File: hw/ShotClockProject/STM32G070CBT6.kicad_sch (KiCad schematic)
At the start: 30 parts, among them J1 Conn_01x06_Pin, J2 Conn_ST_STDC14, SW1 SW_SPDT, U1 STM32G070CBTx, U2 LD39015M33R, Y1 16MHz

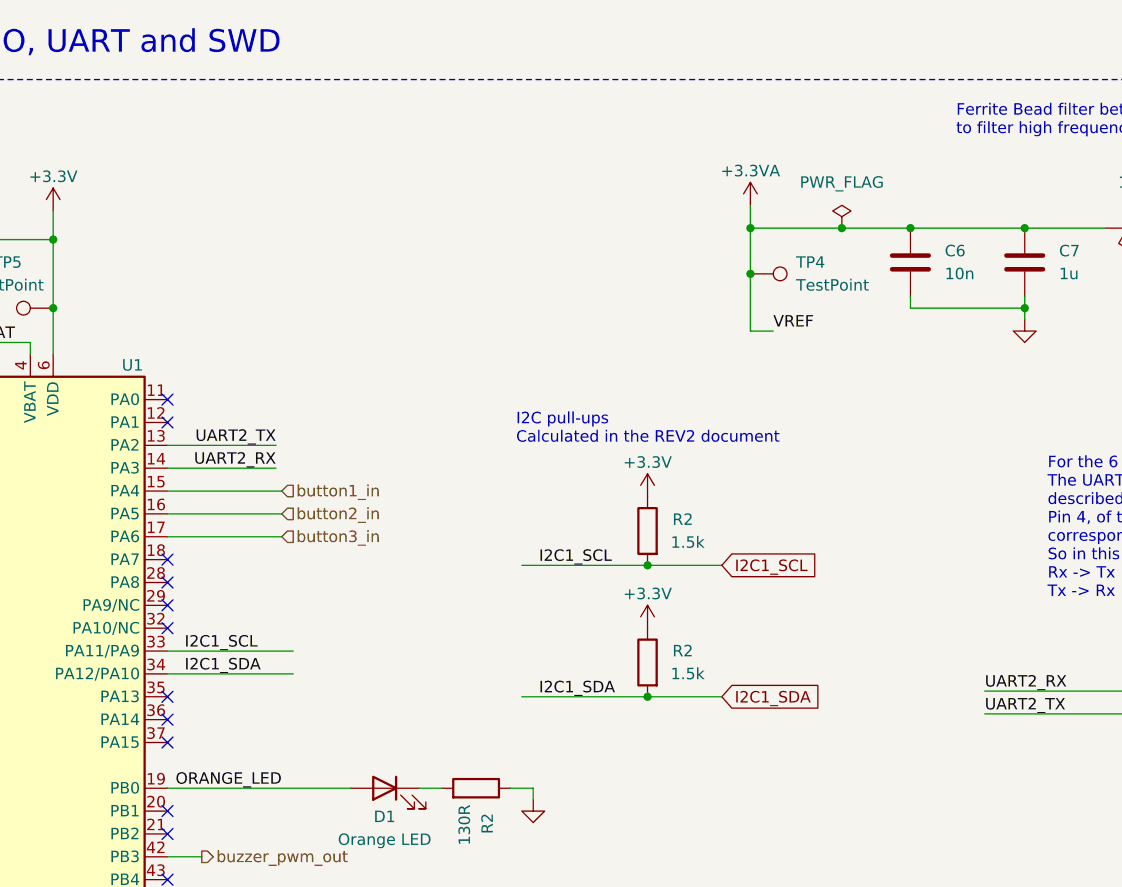
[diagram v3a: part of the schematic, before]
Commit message: Routing on mainboard for LiPo charger
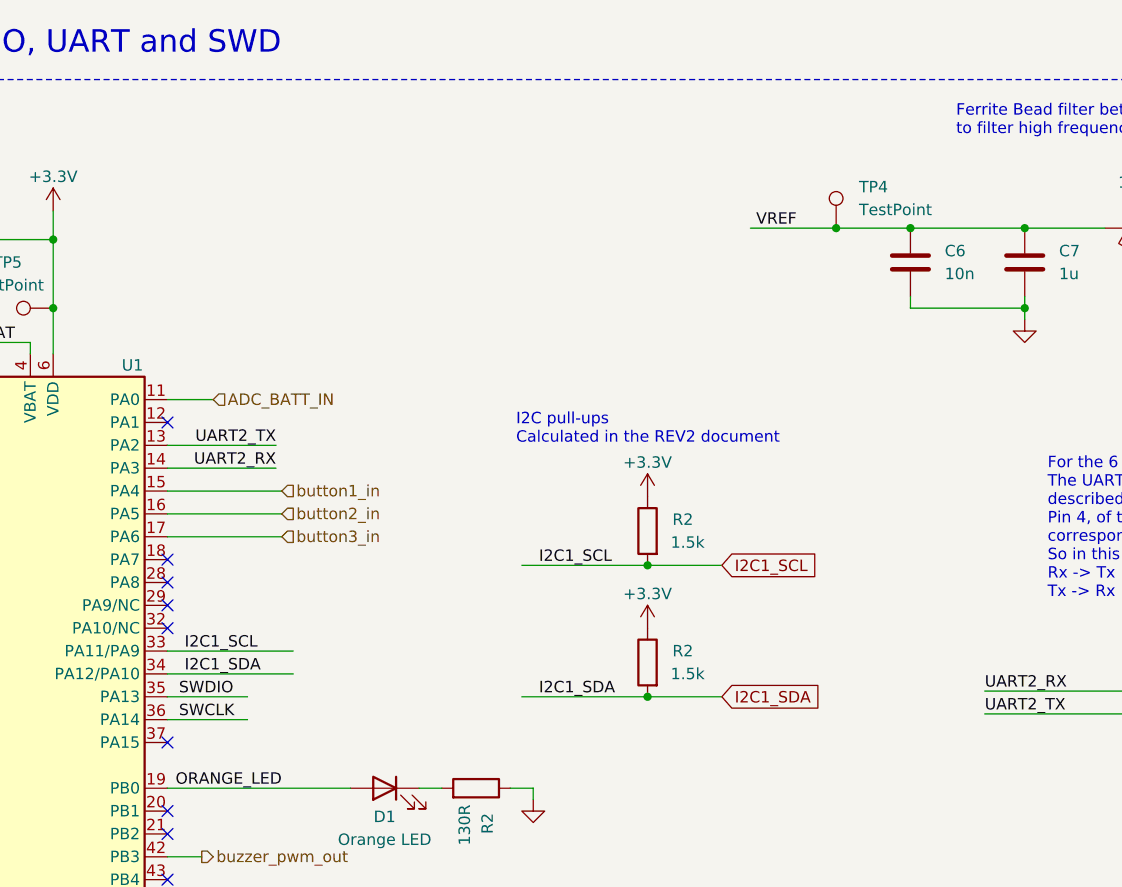
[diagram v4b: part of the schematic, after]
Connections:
- net SWCLK: now also U1.36 (PA14)
- net SWDIO: now also U1.35 (PA13)
- net ADC_BATT_IN: now reaches U1.11 (PA0)
- net +3.3VA renamed VREF
- no-connect marks 34 -> 31
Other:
- moved on the sheet: TP4
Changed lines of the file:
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@@
   (junction (at 226.06 38.1) (diameter 0) (color 0 0 0 0)
   )
-  (junction (at 208.28 38.1) (diameter 0) (color 0 0 0 0)
-  )
   (junction (at 196.85 90.17) (diameter 0) (color 0 0 0 0)
   )
@@
   (junction (at 130.81 46.99) (diameter 0) (color 0 0 0 0)
   )
-  (junction (at 218.44 38.1) (diameter 0) (color 0 0 0 0)
-  )
   (junction (at 81.28 127) (diameter 0) (color 0 0 0 0)
   )
   (junction (at 41.275 127) (diameter 0) (color 0 0 0 0)
   )
+  (junction (at 217.805 38.1) (diameter 0) (color 0 0 0 0)
+  )
   (junction (at 51.435 127) (diameter 0) (color 0 0 0 0)
   )
@@
   )
   (junction (at 111.76 39.37) (diameter 0) (color 0 0 0 0)
-  )
-  (junction (at 208.28 43.18) (diameter 0) (color 0 0 0 0)
   )
   (junction (at 262.89 38.1) (diameter 0) (color 0 0 0 0)
@@
   (no_connect (at 143.51 123.19))
   (no_connect (at 143.51 125.73))
-  (no_connect (at 143.51 90.17))
+  (no_connect (at 143.51 95.25))
   (no_connect (at 113.03 95.25))
   (no_connect (at 143.51 113.03))
@@
   (no_connect (at 113.03 80.01))
   (no_connect (at 248.92 132.715))
-  (no_connect (at 143.51 95.25))
   (no_connect (at 263.525 86.995))
   (no_connect (at 263.525 94.615))
@@
   (no_connect (at 113.03 77.47))
   (no_connect (at 143.51 135.89))
-  (no_connect (at 143.51 92.71))
   (no_connect (at 143.51 105.41))
   (no_connect (at 143.51 138.43))
@@
   (no_connect (at 113.03 82.55))
   (no_connect (at 143.51 80.01))
-  (no_connect (at 143.51 57.15))
   (no_connect (at 113.03 74.93))
   (wire (pts (xy 130.81 52.07) (xy 130.81 46.99))
@@
     (stroke (width 0) (type default))
   )
-  (wire (pts (xy 208.28 38.1) (xy 208.28 43.18))
-    (stroke (width 0) (type default))
-  )
   (wire (pts (xy 130.81 36.195) (xy 130.81 39.37))
     (stroke (width 0) (type default))
@@
     (stroke (width 0) (type default))
   )
-  (wire (pts (xy 218.44 38.1) (xy 226.06 38.1))
+  (wire (pts (xy 208.28 38.1) (xy 217.805 38.1))
     (stroke (width 0) (type default))
   )
@@
     (stroke (width 0) (type default))
   )
+  (wire (pts (xy 143.51 90.17) (xy 152.4 90.17))
+    (stroke (width 0) (type default))
+  )
   (wire (pts (xy 55.88 74.93) (xy 55.88 78.74))
     (stroke (width 0) (type default))
@@
     (stroke (width 0) (type default))
   )
+  (wire (pts (xy 217.805 38.1) (xy 226.06 38.1))
+    (stroke (width 0) (type default))
+  )
   (wire (pts (xy 69.85 137.16) (xy 69.85 139.7))
     (stroke (width 0) (type default))
@@
     (stroke (width 0) (type default))
   )
+  (wire (pts (xy 143.51 57.15) (xy 148.59 57.15))
+    (stroke (width 0) (type default))
+  )
   (wire (pts (xy 155.575 64.77) (xy 143.51 64.77))
     (stroke (width 0) (type default))
@@
     (stroke (width 0) (type default))
   )
+  (wire (pts (xy 143.51 92.71) (xy 152.4 92.71))
+    (stroke (width 0) (type default))
+  )
   (wire (pts (xy 31.75 95.25) (xy 31.75 99.06))
     (stroke (width 0) (type default))
@@
     (stroke (width 0) (type default))
   )
-  (wire (pts (xy 208.28 43.18) (xy 208.28 49.53))
-    (stroke (width 0) (type default))
-  )
   (wire (pts (xy 143.51 87.63) (xy 157.48 87.63))
     (stroke (width 0) (type default))
@@
     (stroke (width 0) (type default))
   )
-  (wire (pts (xy 208.28 35.56) (xy 208.28 38.1))
-    (stroke (width 0) (type default))
-  )
   (wire (pts (xy 236.855 140.335) (xy 248.92 140.335))
     (stroke (width 0) (type default))
@@
     (stroke (width 0) (type default))
   )
-  (wire (pts (xy 208.28 38.1) (xy 218.44 38.1))
-    (stroke (width 0) (type default))
-  )
   (wire (pts (xy 81.28 136.525) (xy 92.075 136.525))
     (stroke (width 0) (type default))
   )
   (wire (pts (xy 34.29 73.66) (xy 97.79 73.66))
-    (stroke (width 0) (type default))
-  )
-  (wire (pts (xy 208.28 49.53) (xy 210.82 49.53))
     (stroke (width 0) (type default))
   )
@@
     (effects (font (size 1.27 1.27)) (justify left bottom))
   )
+  (label "SWDIO" (at 144.78 90.17 0) (fields_autoplaced)
+    (effects (font (size 1.27 1.27)) (justify left bottom))
+  )
   (label "UART2_TX" (at 155.575 62.23 180) (fields_autoplaced)
     (effects (font (size 1.27 1.27)) (justify right bottom))
@@
     (effects (font (size 1.27 1.27)) (justify left bottom))
   )
-  (label "VREF" (at 210.82 49.53 0) (fields_autoplaced)
+  (label "VREF" (at 208.915 38.1 0) (fields_autoplaced)
     (effects (font (size 1.27 1.27)) (justify left bottom))
   )
@@
   )
   (label "UART1_RX" (at 236.855 137.795 0) (fields_autoplaced)
+    (effects (font (size 1.27 1.27)) (justify left bottom))
+  )
+  (label "SWCLK" (at 144.78 92.71 0) (fields_autoplaced)
     (effects (font (size 1.27 1.27)) (justify left bottom))
   )
@@
   )
   (hierarchical_label "button2_in" (shape input) (at 156.21 69.85 0) (fields_autoplaced)
+    (effects (font (size 1.27 1.27)) (justify left))
+  )
+  (hierarchical_label "ADC_BATT_IN" (shape input) (at 148.59 57.15 0) (fields_autoplaced)
     (effects (font (size 1.27 1.27)) (justify left))
   )
@@
         (path "/5fd859aa-754d-49c2-9762-3f7ebe3bb64c/5bec211e-466d-46c6-9543-84cb75088ef1"
           (reference "TP5") (unit 1)
-        )
-      )
-    )
-  )
-  (symbol (lib_id "power:PWR_FLAG") (at 218.44 38.1 0) (unit 1)
-    (in_bom yes) (on_board yes) (dnp no) (fields_autoplaced)
-    (property "Reference" "#FLG04" (at 218.44 36.195 0)
-      (effects (font (size 1.27 1.27)) hide)
-    )
-    (property "Value" "PWR_FLAG" (at 218.44 33.02 0)
-      (effects (font (size 1.27 1.27)))
-    )
-    (property "Footprint" "" (at 218.44 38.1 0)
-      (effects (font (size 1.27 1.27)) hide)
-    )
-    (property "Datasheet" "~" (at 218.44 38.1 0)
-      (effects (font (size 1.27 1.27)) hide)
-    )
-    (pin "1")
-    (instances
-      (project "ShotClockProject"
-        (path "/5fd859aa-754d-49c2-9762-3f7ebe3bb64c/d287d155-1951-4d4f-8d6c-570f03bc79f5"
-          (reference "#FLG04") (unit 1)
-        )
-        (path "/5fd859aa-754d-49c2-9762-3f7ebe3bb64c/17367eb9-0f4d-4017-b1ca-d50430410a5d"
-          (reference "#FLG04") (unit 1)
-        )
-        (path "/5fd859aa-754d-49c2-9762-3f7ebe3bb64c/5bec211e-466d-46c6-9543-84cb75088ef1"
-          (reference "#FLG03") (unit 1)
         )
       )
@@
     )
   )
-  (symbol (lib_id "Connector:TestPoint") (at 208.28 43.18 270) (unit 1)
+  (symbol (lib_id "Connector:TestPoint") (at 217.805 38.1 0) (unit 1)
     (in_bom yes) (on_board yes) (dnp no) (fields_autoplaced)
-    (property "Reference" "TP4" (at 213.36 41.91 90)
-      (effects (font (size 1.27 1.27)) (justify left))
-    )
-    (property "Value" "TestPoint" (at 213.36 44.45 90)
-      (effects (font (size 1.27 1.27)) (justify left))
-    )
-    (property "Footprint" "TestPoint:TestPoint_Pad_D1.0mm" (at 208.28 48.26 0)
-      (effects (font (size 1.27 1.27)) hide)
-    )
-    (property "Datasheet" "~" (at 208.28 48.26 0)
-      (effects (font (size 1.27 1.27)) hide)
-    )
-    (property "LCSC Part #" "" (at 208.28 43.18 0)
-      (effects (font (size 1.27 1.27)) hide)
-    )
-    (property "LCSC Part" "" (at 208.28 43.18 0)
+    (property "Reference" "TP4" (at 220.345 33.528 0)
+      (effects (font (size 1.27 1.27)) (justify left))
+    )
+    (property "Value" "TestPoint" (at 220.345 36.068 0)
+      (effects (font (size 1.27 1.27)) (justify left))
+    )
+    (property "Footprint" "TestPoint:TestPoint_Pad_D1.0mm" (at 222.885 38.1 0)
+      (effects (font (size 1.27 1.27)) hide)
+    )
+    (property "Datasheet" "~" (at 222.885 38.1 0)
+      (effects (font (size 1.27 1.27)) hide)
+    )
+    (property "LCSC Part #" "" (at 217.805 38.1 0)
+      (effects (font (size 1.27 1.27)) hide)
+    )
+    (property "LCSC Part" "" (at 217.805 38.1 0)
       (effects (font (size 1.27 1.27)) hide)
     )
@@
         )
       )
-    )
-  )
-  (symbol (lib_id "power:+3.3VA") (at 208.28 35.56 0) (unit 1)
-    (in_bom yes) (on_board yes) (dnp no)
-    (property "Reference" "#PWR04" (at 208.28 39.37 0)
-      (effects (font (size 1.27 1.27)) hide)
-    )
-    (property "Value" "+3.3VA" (at 208.28 31.75 0)
-      (effects (font (size 1.27 1.27)))
-    )
-    (property "Footprint" "" (at 208.28 35.56 0)
-      (effects (font (size 1.27 1.27)) hide)
-    )
-    (property "Datasheet" "" (at 208.28 35.56 0)
-      (effects (font (size 1.27 1.27)) hide)
-    )
-    (pin "1")
-    (instances
-      (project "ShotClockProject"
-        (path "/5fd859aa-754d-49c2-9762-3f7ebe3bb64c"
-          (reference "#PWR04") (unit 1)
-        )
-        (path "/5fd859aa-754d-49c2-9762-3f7ebe3bb64c/5bec211e-466d-46c6-9543-84cb75088ef1"
-          (reference "#PWR03") (unit 1)
-        )
-      )

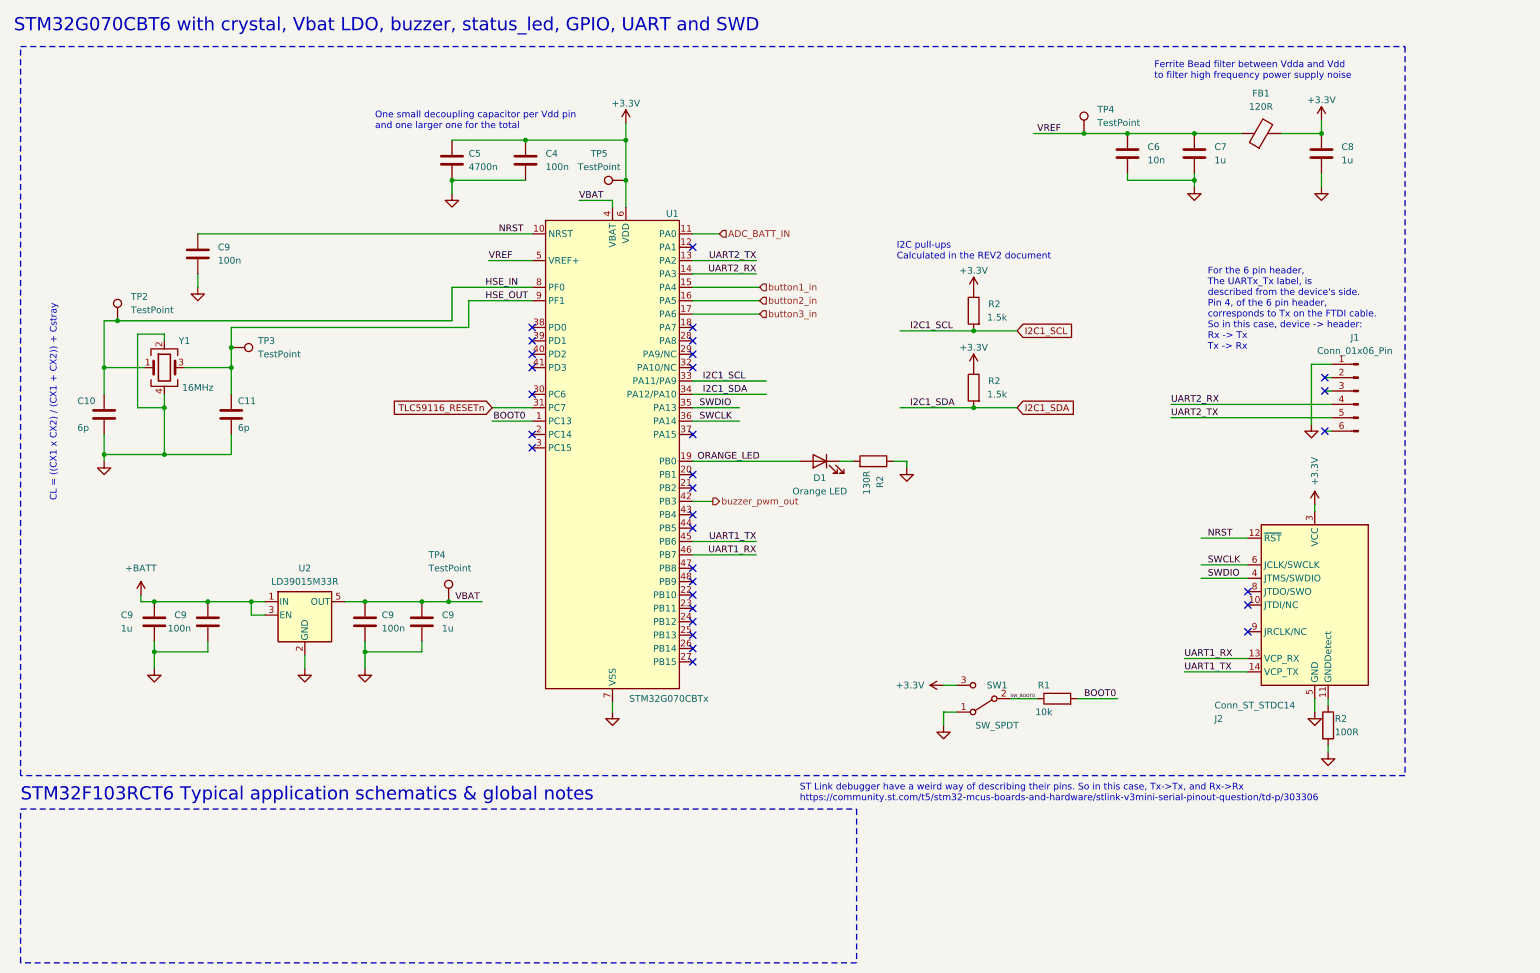
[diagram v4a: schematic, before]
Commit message: Finished mainboard routing
Reconfigered pins to make routing easier/cleaner
Placed copper fills as much as possible to create an even plating index
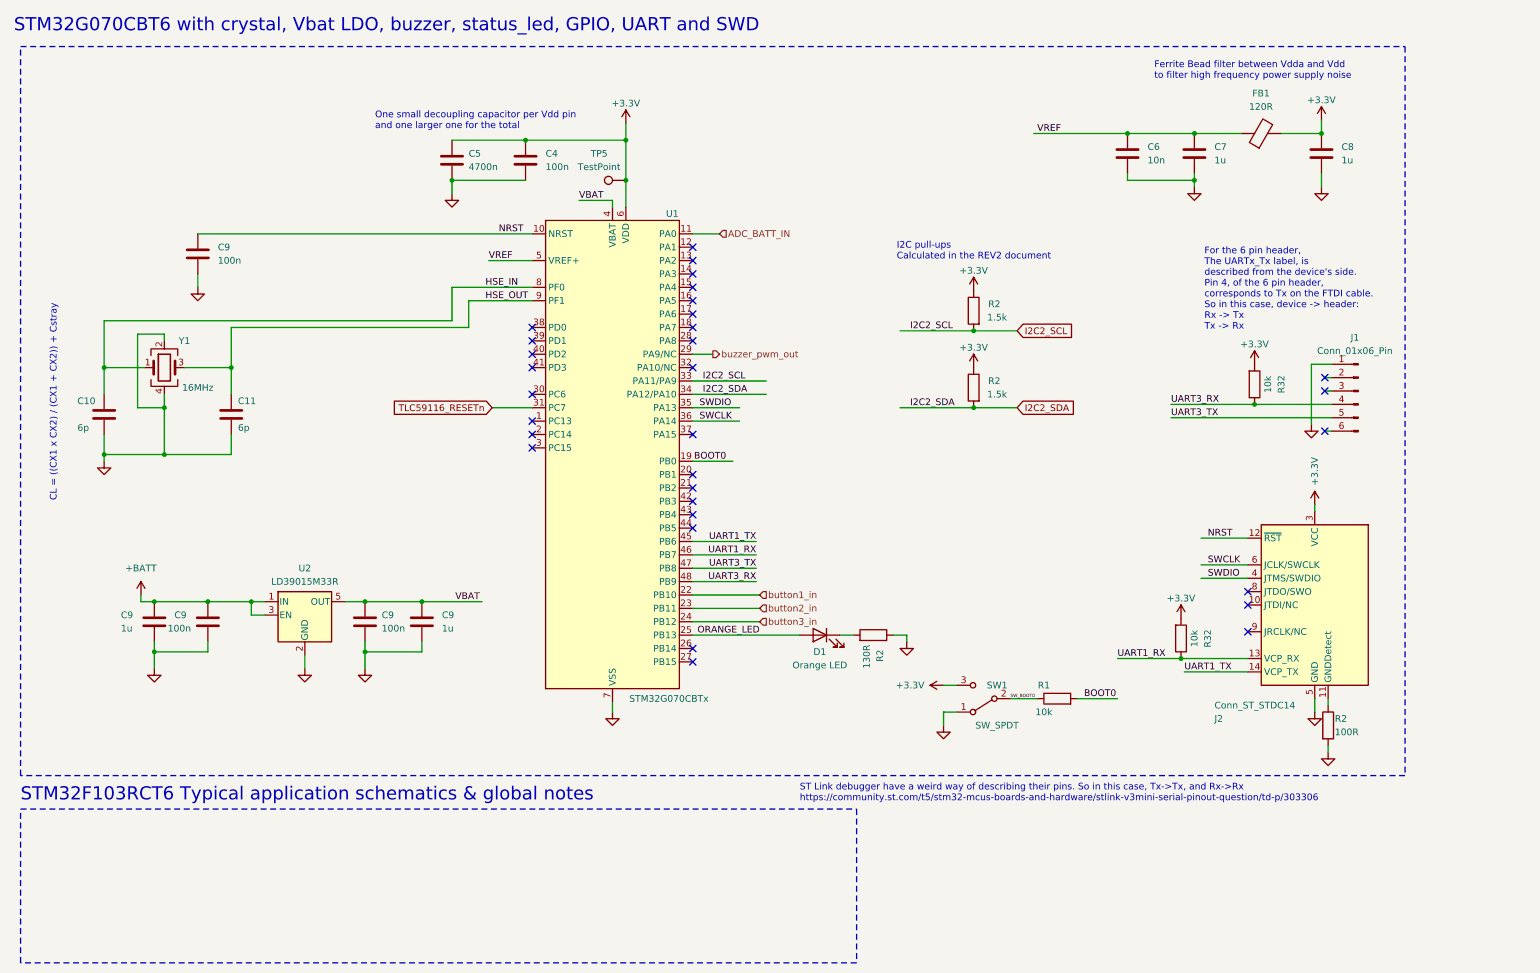
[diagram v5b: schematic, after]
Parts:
- removed TP2, TP3, TP4 (x2): TestPoint, TestPoint:TestPoint_Pad_D1.0mm, symbol Connector:TestPoint
- added R32 (x2): 10k, Resistor_SMD:R_0402_1005Metric, symbol Device:R
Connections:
- net +3.3V: now also R32.2, R32.2
- net BOOT0: now also U1.19 (PB0); no longer U1.1 (PC13)
- net ORANGE_LED: now also U1.25 (PB13); no longer U1.19 (PB0)
- net UART1_RX: now also R32.1
- net button1_in: now also U1.22 (PB10); no longer U1.15 (PA4)
- net button2_in: now also U1.23 (PB11); no longer U1.16 (PA5)
- net button3_in: now also U1.24 (PB12); no longer U1.17 (PA6)
- net buzzer_pwm_out: now also U1.29 (PA9/NC); no longer U1.42 (PB3)
- net UART3_TX: now reaches U1.47 (PB8)
- net UART3_TX: now also J1.5 (Pin_5)
- net UART3_RX: now reaches U1.48 (PB9)
- net UART3_RX: now also J1.4 (Pin_4), R32.1
- net I2C1_SCL renamed I2C2_SCL
- net I2C1_SDA renamed I2C2_SDA
- net UART2_RX: no longer names the net of U1.14 (PA3)
- net UART2_RX: no longer J1.4 (Pin_4)
- net UART2_TX: no longer names the net of U1.13 (PA2)
- net UART2_TX: no longer J1.5 (Pin_5)
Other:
- moved on the sheet: D1, R2
